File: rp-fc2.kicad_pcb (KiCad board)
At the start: 4 copper layers, 45 x 75 mm, 32 parts, among them CN1 20021521-00010T1LF, SW1 SW_Push, U1 RP2350A-QFN60, U2 W25Q128JVS, Y1 Crystal_GND24

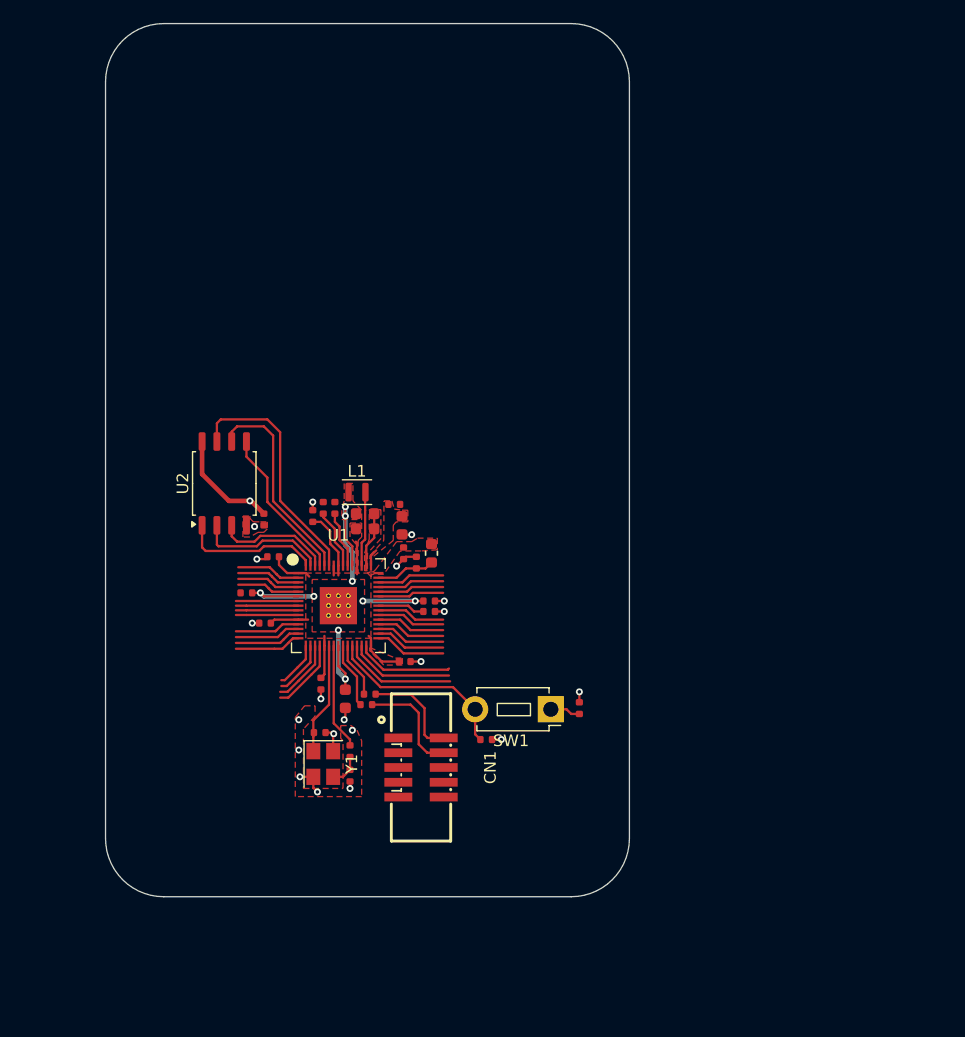
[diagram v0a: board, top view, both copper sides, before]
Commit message: rp2350 power + servo rails
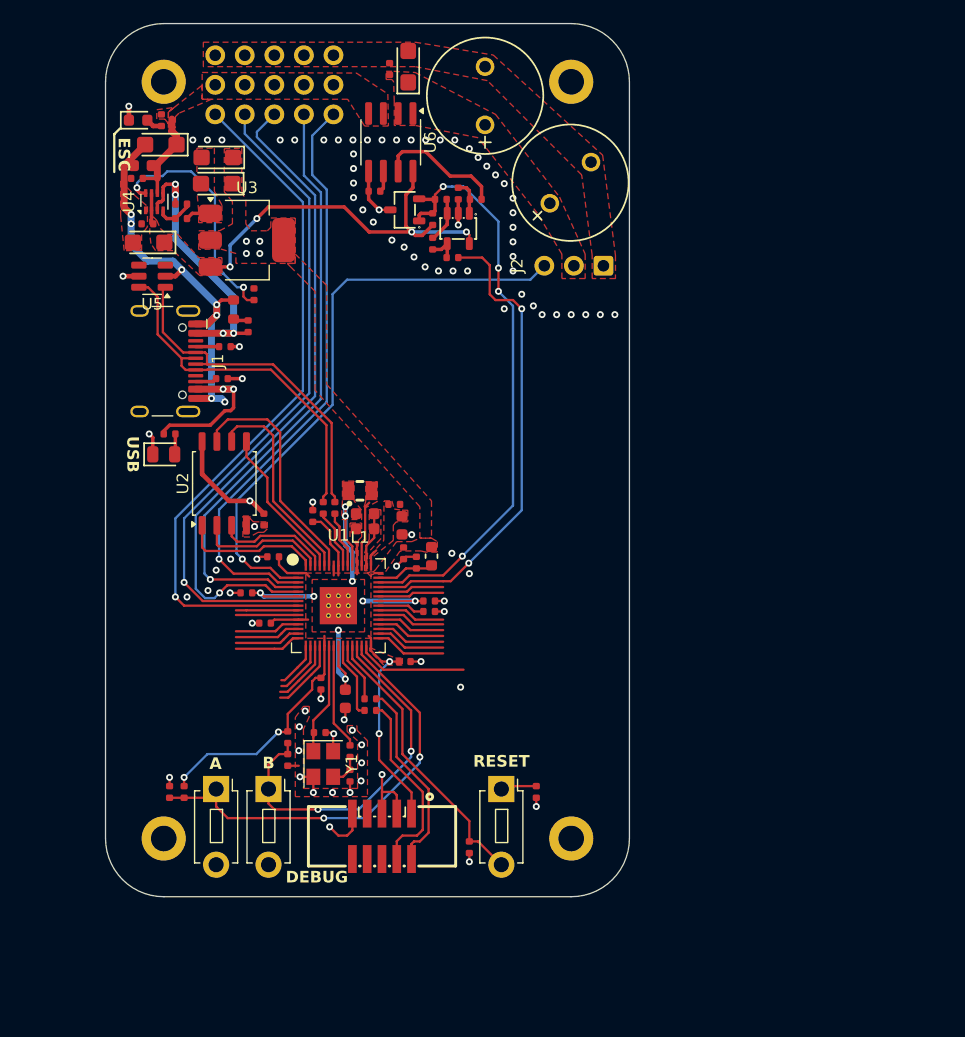
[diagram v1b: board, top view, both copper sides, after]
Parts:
- added C19: 100nF, PCM_JLCPCB:C_0402, F.Cu at (103.6, 92.2)
- added C20: 10uF, PCM_JLCPCB:C_CASE-A-3216-18(mm), F.Cu at (103.7, 93.8)
- added C21: 10uF, PCM_JLCPCB:C_CASE-A-3216-18(mm), F.Cu at (109.6, 86.5)
- added C22: 10uF, PCM_JLCPCB:C_CASE-A-3216-18(mm), F.Cu at (109.5, 88.8)
- added C23: 10uF, PCM_JLCPCB:C_CASE-A-3216-18(mm), F.Cu at (126.0, 78.7)
- added C24: 470uF, PCM_JLCPCB:C_Plugin,D10xL16mm, F.Cu at (132.6, 81.2)
- added C25: 470uF, PCM_JLCPCB:C_Plugin,D10xL16mm, F.Cu at (139.9, 88.7)
- added C26: 100nF, PCM_JLCPCB:C_0402, F.Cu at (124.4, 78.9)
- added C27: 100nF, PCM_JLCPCB:C_0402, F.Cu at (123.1, 89.4)
- added C28: 100nF, PCM_JLCPCB:C_0402, F.Cu at (102.7, 88.3)
- added C29: 2.2uF, PCM_JLCPCB:C_0603, F.Cu at (103.2, 87.2)
- added C30: 10uF, PCM_JLCPCB:C_CASE-A-3216-18(mm), F.Cu at (104.8, 85.4)
- added C31: 100nF, PCM_JLCPCB:C_0402, F.Cu at (105.5, 141.0)
- added C32: 100nF, PCM_JLCPCB:C_0402, F.Cu at (115.7, 138.2)
- added D1: Red, PCM_JLCPCB:D_0805, F.Cu at (105.0, 112.0)
- added D2: Red, PCM_JLCPCB:D_0603, F.Cu at (102.8, 83.3)
- added H1: MountingHole_Pad, MountingHole:MountingHole_2.2mm_M2_DIN965_Pad, F.Cu at (105.0, 80.0)
- added H2: MountingHole_Pad, MountingHole:MountingHole_2.2mm_M2_DIN965_Pad, F.Cu at (140.0, 80.0)
- added H3: MountingHole_Pad, MountingHole:MountingHole_2.2mm_M2_DIN965_Pad, F.Cu at (105.0, 145.0)
- added H4: MountingHole_Pad, MountingHole:MountingHole_2.2mm_M2_DIN965_Pad, F.Cu at (140.0, 145.0)
- added J1: USB_C_Receptacle_USB2.0_16P, Connector_USB:USB_C_Receptacle_HCTL_HC-TYPE-C-16P-01A, F.Cu at (104.0, 104.0)
- added J2: Conn_01x03, Connector_PinHeader_2.54mm:PinHeader_1x03_P2.54mm_Vertical, F.Cu at (137.7, 95.8)
- added J3: Conn_01x05, Connector_PinHeader_2.54mm:PinHeader_1x05_P2.54mm_Vertical, F.Cu at (109.4, 82.8)
- added J4: Conn_01x05, Connector_PinHeader_2.54mm:PinHeader_1x05_P2.54mm_Vertical, F.Cu at (109.4, 80.3)
- added J5: Conn_01x05, Connector_PinHeader_2.54mm:PinHeader_1x05_P2.54mm_Vertical, F.Cu at (109.4, 77.7)
- added R10: 220Ω, PCM_JLCPCB:R_0402, F.Cu at (105.5, 110.2)
- added R11: 5.1kΩ, PCM_JLCPCB:R_0402, F.Cu at (110.0, 105.5)
- added R12: 10kΩ, PCM_JLCPCB:R_0402, F.Cu at (106.5, 91.8)
- added R13: 10kΩ, PCM_JLCPCB:R_0402, F.Cu at (112.8, 98.2)
- added R14: 33kΩ, PCM_JLCPCB:R_0402, F.Cu at (112.2, 101.0)
- added R15: 82kΩ, PCM_JLCPCB:R_0603, F.Cu at (111.0, 99.6)
- added R16: 10kΩ, PCM_JLCPCB:R_0402, F.Cu at (131.8, 90.1)
- added R17: 27kΩ, PCM_JLCPCB:R_0402, F.Cu at (130.3, 89.6)
- added R18: 680Ω, PCM_JLCPCB:R_0402, F.Cu at (128.1, 91.8)
- added R19: 220Ω, PCM_JLCPCB:R_0402, F.Cu at (129.8, 95.1)
- added R20: 10kΩ, PCM_JLCPCB:R_0402, F.Cu at (128.8, 90.1)
- added R21: 27kΩ, PCM_JLCPCB:R_0402, F.Cu at (128.1, 93.9)
- added R22: 220Ω, PCM_JLCPCB:R_0402, F.Cu at (104.8, 83.3)
- added R23: 10kΩ, PCM_JLCPCB:R_0402, F.Cu at (106.8, 141.0)
- added R24: 10kΩ, PCM_JLCPCB:R_0402, F.Cu at (115.7, 136.3)
- added R8: 5.1kΩ, PCM_JLCPCB:R_0402, F.Cu at (110.2, 102.8)
- added R9: 10kΩ, PCM_JLCPCB:R_0402, F.Cu at (106.5, 90.5)
- added SW2: SW_Push, Button_Switch_THT:SW_PUSH_1P1T_6x3.5mm_H4.3_APEM_MJTP1243, F.Cu at (109.5, 140.8)
- added SW3: SW_Push, Button_Switch_THT:SW_PUSH_1P1T_6x3.5mm_H4.3_APEM_MJTP1243, F.Cu at (114.0, 140.8)
- added U3: AMS1117-3.3, Package_TO_SOT_SMD:SOT-223-3_TabPin2, F.Cu at (112.2, 93.6)
- added U4: TPS2116DRL, Package_TO_SOT_SMD:SOT-583-8, F.Cu at (104.2, 90.3)
- added U5: SRV05-4, Package_TO_SOT_SMD:SOT-23-6, F.Cu at (104.0, 96.7)
- added U6: ACS712xLCTR-05B, Package_SO:SOIC-8_3.9x4.9mm_P1.27mm, F.Cu at (124.5, 85.2)
- added U7: LMV321IDBVR, PCM_JLCPCB:SOT-23-5_L3.0-W1.7-P0.95-LS2.8-BR, F.Cu at (130.3, 92.6)
- added U8: CJ431, PCM_JLCPCB:SOT-23-3_L2.9-W1.6-P1.90-LS2.8-BR, F.Cu at (125.7, 91.0)
- L1: value 3.3u -> AOTA-B201610S3R3-101-T; footprint Inductor_SMD:L_Murata_DFE201610P -> easyeda2kicad:IND-SMD_L2.0-W1.6_AOTA-B201610S3R3-101-T
- moved C18 9.36 mm to (131.2, 145.8), turned to -90 degrees
- moved R4 8.10 mm to (137.0, 141.0), turned to 90 degrees
- moved SW1 8.06 mm to (134.0, 140.8), turned to -90 degrees
- moved CN1 6.80 mm to (123.7, 144.8), turned to 180 degrees
- moved R6 0.61 mm to (122.8, 134.0)
- moved R7 0.40 mm to (122.8, 133.0)
- moved L1 0.28 mm to (121.8, 115.1), turned to 180 degrees
- moved FB1 0.25 mm to (128.0, 120.8)
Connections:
- CN1 pad 7: GND -> unconnected-(CN1-Pad7)
- L1 pad 1: +1V1 -> Net-(U1-VREG_LX)
- L1 pad 2: Net-(U1-VREG_LX) -> +1V1
- U1 pad 2: unconnected-(U1-GPIO0-Pad2) -> CH1
- U1 pad 27: unconnected-(U1-GPIO16-Pad27) -> USR_SW1
- U1 pad 28: unconnected-(U1-GPIO17-Pad28) -> USR_SW2
- U1 pad 3: unconnected-(U1-GPIO1-Pad3) -> CH6
- U1 pad 4: unconnected-(U1-GPIO2-Pad4) -> CH5
- U1 pad 42: unconnected-(U1-GPIO28_ADC2-Pad42) -> I_COND
- U1 pad 43: unconnected-(U1-GPIO29_ADC3-Pad43) -> I_COND_2_5
- U1 pad 5: unconnected-(U1-GPIO3-Pad5) -> CH4
- U1 pad 7: unconnected-(U1-GPIO4-Pad7) -> CH3
- U1 pad 8: unconnected-(U1-GPIO5-Pad8) -> CH2
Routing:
- net GND: track 21.4 -> 84.6 mm, vias 20 -> 97
- net CH2: track 0.00 -> 60.0 mm, vias 0 -> 1
- net CH4: track 0.00 -> 57.5 mm, vias 0 -> 1
- net CH3: track 0.00 -> 57.4 mm, vias 0 -> 1
- net CH5: track 0.00 -> 52.7 mm, vias 0 -> 1
- net CH1: track 0.00 -> 51.1 mm, vias 0 -> 1
- net I_COND_2_5: track 0.00 -> 51.0 mm, vias 0 -> 4
- net CH6: track 0.00 -> 50.9 mm, vias 0 -> 1
- net I_COND: track 0.00 -> 41.1 mm, vias 0 -> 2
- net /Power/USB_VBUS: track 0.00 -> 39.7 mm, vias 0 -> 7
- net +5V: track 0.00 -> 37.9 mm, vias 0 -> 4
- net USR_SW2: track 0.00 -> 37.8 mm, vias 0 -> 2
- net USR_SW1: track 0.00 -> 32.1 mm, vias 0 -> 2
- net +3V3: track 38.1 -> 70.0 mm, vias 1 -> 9
- net USB_D+: track 0.00 -> 31.2 mm
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- added copper zone on F.Cu, net +5V
- added copper zone on F.Cu, net /Power/VBUCK_IN
- added copper zone on F.Cu, net Net-(U1-VREG_LX)
- added copper zone on F.Cu, net VBUCK
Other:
- board text added: "A"
- board text added: "B"
- board text added: "DEBUG"
- board text added: "ESC"
- board text added: "RESET"
- board text added: "USB"

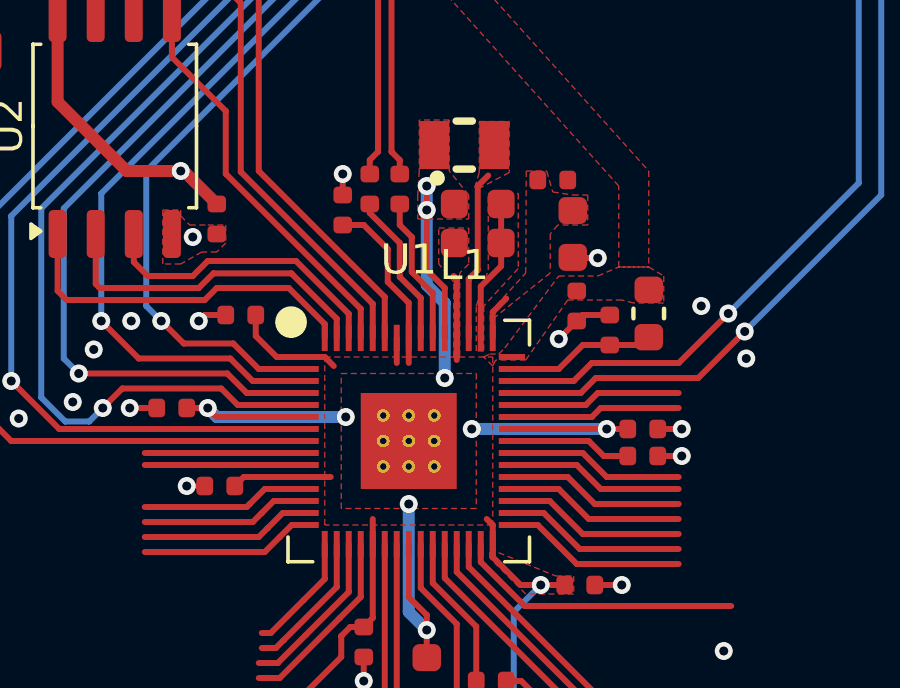
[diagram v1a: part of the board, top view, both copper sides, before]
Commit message: 3v3 rail thicker
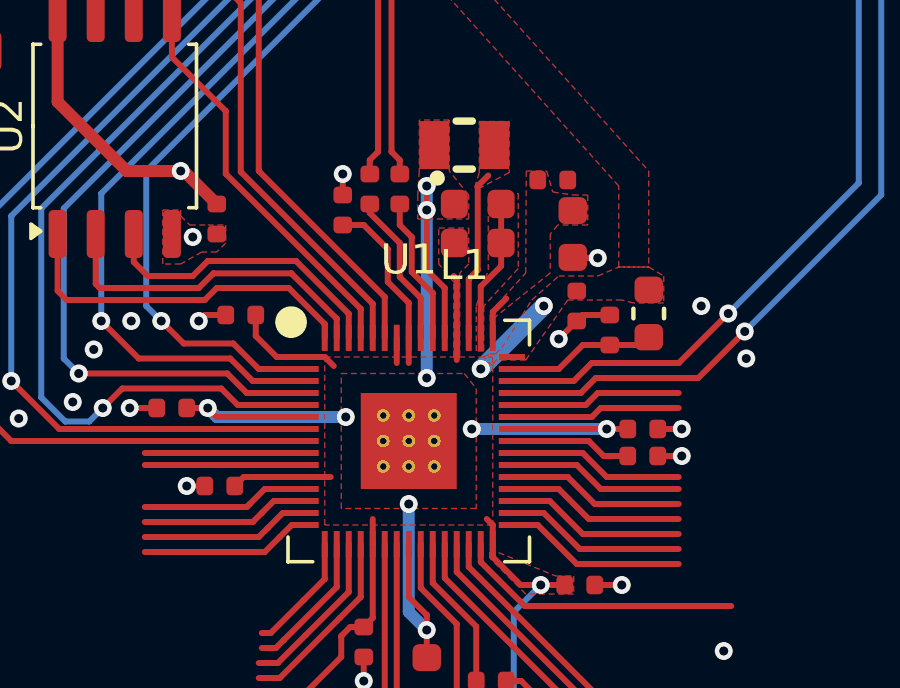
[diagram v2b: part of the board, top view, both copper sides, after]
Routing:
- net +3V3: track 70.0 -> 73.0 mm, vias 9 -> 11
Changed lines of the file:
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@@
 			(dashed_line_gap_ratio 3.000000)
 			(svgprecision 4)
-			(plotframeref no)
+			(plotframeref yes)
 			(viasonmask no)
 			(mode 1)
@@
 	)
 	(via
+		(at 122.4 122.6)
+		(size 0.6)
+		(drill 0.3)
+		(layers "F.Cu" "B.Cu")
+		(free yes)
+		(net 3)
+	)
+	(via
+		(at 124.5 120.5)
+		(size 0.6)
+		(drill 0.3)
+		(layers "F.Cu" "B.Cu")
+		(free yes)
+		(net 3)
+	)
+	(via
 		(at 113.25 93.7)
 		(size 0.6)
@@
 	)
 	(segment
+		(start 124.5 120.5)
+		(end 122.4 122.6)
+		(width 0.6)
+		(layer "B.Cu")
+		(net 3)
+	)
+	(segment
 		(start 114.85 135.85)
 		(end 112.95 137.75)
@@
 	)
 	(via
-		(at 121.2 122.9)
+		(at 120.6 122.899998)
 		(size 0.6)
 		(drill 0.3)
@@
 	)
 	(segment
-		(start 120.6 119.8)
-		(end 121.2 120.4)
-		(width 0.4)
-		(layer "B.Cu")
-		(net 4)
-	)
-	(segment
-		(start 121.2 120.4)
-		(end 121.2 122.9)
-		(width 0.4)
-		(layer "B.Cu")
-		(net 4)
-	)
-	(segment
 		(start 122.1 124.6)
 		(end 126.6 124.6)
@@
 	)
 	(segment
-		(start 113.3 123.9)
-		(end 113.6 124.2)
+		(start 120.6 122.899998)
+		(end 120.6 116.5)
 		(width 0.4)
 		(layer "B.Cu")
@@
 	)
 	(segment
-		(start 120.6 116.5)
-		(end 120.6 119.8)
+		(start 113.3 123.9)
+		(end 113.6 124.2)
 		(width 0.4)
 		(layer "B.Cu")
@@
 		(polygon
 			(pts
-				(xy 117.75 122.75) (xy 122.25 122.75) (xy 122.25 127.25) (xy 117.75 127.25)
+				(xy 117.75 122.75) (xy 121.85 122.75) (xy 122.25 123.25) (xy 122.25 127.25) (xy 117.75 127.25)
 			)
 		)
@@
 		(polygon
 			(pts
-				(xy 122.5 122.2) (xy 122.7 122.1) (xy 123 122.1) (xy 123.2 121.9) (xy 125 119.5) (xy 126.3 119.5)
-				(xy 127 119.2) (xy 128 119.2) (xy 128.5 119.5) (xy 128.5 120.4) (xy 127.5 120.4) (xy 127.1 120.3)
-				(xy 125.3 120.3) (xy 123.9 122.3) (xy 122.9 122.3) (xy 122.8 122.5)
+				(xy 122.5 122.2) (xy 122.7 122.1) (xy 122.9 122.1) (xy 123.1 121.9) (xy 124.1 120.3) (xy 125 119.5)
+				(xy 126.3 119.5) (xy 127 119.2) (xy 128 119.2) (xy 128.5 119.5) (xy 128.5 120.4) (xy 127.5 120.4)
+				(xy 127.1 120.3) (xy 125.3 120.3) (xy 123.9 122.3) (xy 122.9 122.3) (xy 122.8 122.5)
 			)
 		)

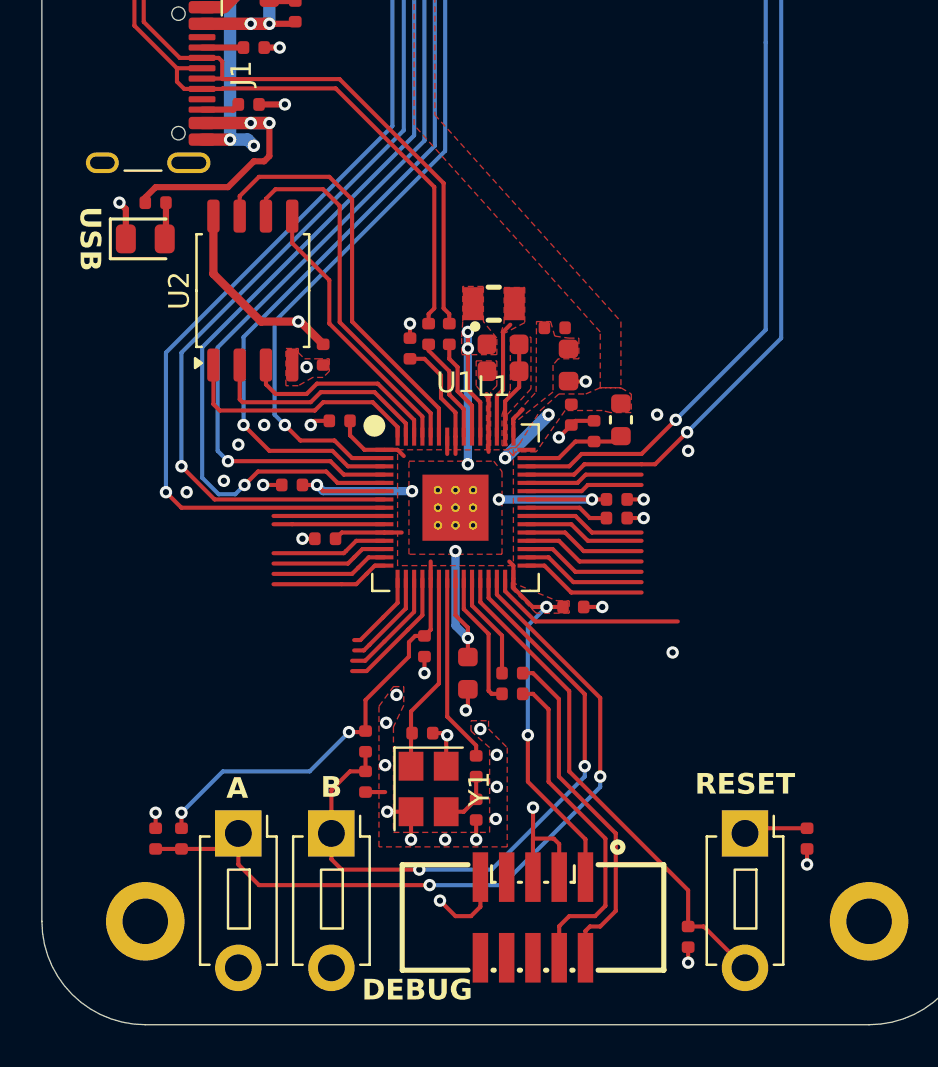
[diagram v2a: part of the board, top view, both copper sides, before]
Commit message: add camera breakout
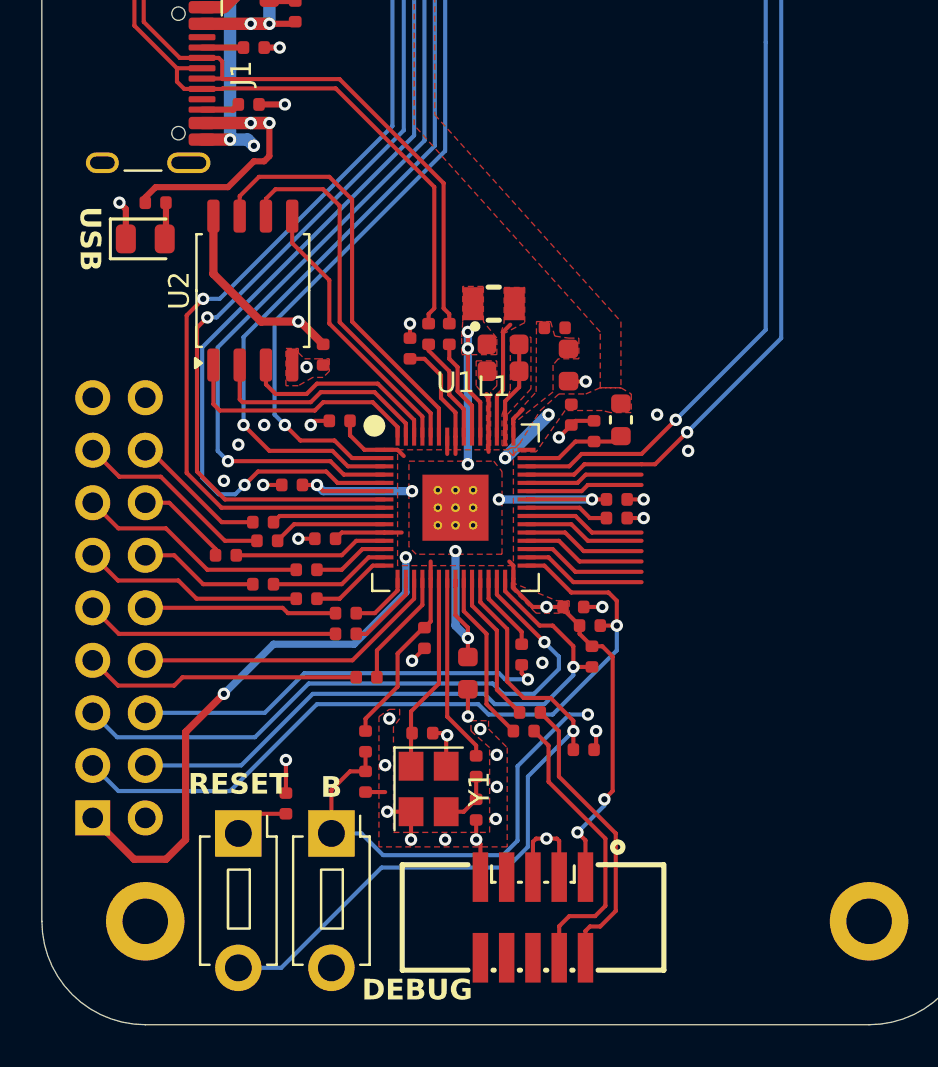
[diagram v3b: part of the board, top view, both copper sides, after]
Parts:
- removed C31: 100nF, PCM_JLCPCB:C_0402
- removed SW2: SW_Push, Button_Switch_THT:SW_PUSH_1P1T_6x3.5mm_H4.3_APEM_MJTP1243
- added J6: OV7670 Breakout, Connector_PinHeader_2.54mm:PinHeader_2x09_P2.54mm_Vertical, B.Cu at (102.5, 140.0)
- added R25: 22Ω, PCM_JLCPCB:R_0402, F.Cu at (110.9, 126.6)
- added R26: 22Ω, PCM_JLCPCB:R_0402, F.Cu at (108.9, 127.3)
- added R27: 22Ω, PCM_JLCPCB:R_0402, F.Cu at (112.8, 128.0)
- added R28: 22Ω, PCM_JLCPCB:R_0402, F.Cu at (110.7, 128.7)
- added R29: 22Ω, PCM_JLCPCB:R_0402, F.Cu at (112.8, 129.4)
- added R30: 22Ω, PCM_JLCPCB:R_0402, F.Cu at (114.7, 130.1)
- added R31: 22Ω, PCM_JLCPCB:R_0402, F.Cu at (114.7, 131.1)
- added R32: 22Ω, PCM_JLCPCB:R_0402, F.Cu at (115.7, 133.2)
- added R33: 22Ω, PCM_JLCPCB:R_0402, F.Cu at (123.2, 132.1)
- added R34: 4.7kΩ, PCM_JLCPCB:R_0402, F.Cu at (126.6, 132.2)
- added R35: 4.7kΩ, PCM_JLCPCB:R_0402, F.Cu at (126.5, 130.7)
- R23: value 10kΩ -> 22Ω
- moved R4 25.3 mm to (111.8, 139.3), turned to -90 degrees
- moved SW1 24.5 mm to (109.5, 140.8)
- moved R23 15.8 mm to (110.7, 125.7), turned to 180 degrees
- moved C18 10.4 mm to (126.2, 136.7), turned to 0 degrees
- moved R7 2.08 mm to (123.6, 134.9)
- moved R6 1.88 mm to (123.3, 135.8)
- moved C13 0.40 mm to (118.5, 131.3)
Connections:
- R23 pad 1: USR_SW2 -> Net-(U1-GPIO6)
- R23 pad 2: +3V3 -> D0
- U1 pad 10: unconnected-(U1-GPIO7-Pad10) -> Net-(U1-GPIO7)
- U1 pad 12: unconnected-(U1-GPIO8-Pad12) -> Net-(U1-GPIO8)
- U1 pad 13: unconnected-(U1-GPIO9-Pad13) -> Net-(U1-GPIO9)
- U1 pad 14: unconnected-(U1-GPIO10-Pad14) -> Net-(U1-GPIO10)
- U1 pad 15: unconnected-(U1-GPIO11-Pad15) -> Net-(U1-GPIO11)
- U1 pad 16: unconnected-(U1-GPIO12-Pad16) -> Net-(U1-GPIO12)
- U1 pad 17: unconnected-(U1-GPIO13-Pad17) -> Net-(U1-GPIO13)
- U1 pad 18: unconnected-(U1-GPIO14-Pad18) -> XCLK
- U1 pad 19: unconnected-(U1-GPIO15-Pad19) -> Net-(U1-GPIO15)
- U1 pad 27: USR_SW1 -> Net-(U1-GPIO16)
- U1 pad 28: USR_SW2 -> VSYNC
- U1 pad 29: unconnected-(U1-GPIO18-Pad29) -> SIO_D
- U1 pad 31: unconnected-(U1-GPIO19-Pad31) -> SIO_C
- U1 pad 32: unconnected-(U1-GPIO20-Pad32) -> USR_SW1
- U1 pad 9: unconnected-(U1-GPIO6-Pad9) -> Net-(U1-GPIO6)
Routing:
- net USR_SW2: track 37.8 -> 0.00 mm, vias 2 -> 0
- net SIO_C: track 0.00 -> 37.4 mm, vias 0 -> 1
- net VSYNC: track 0.00 -> 30.4 mm, vias 0 -> 1
- net SIO_D: track 0.00 -> 30.2 mm, vias 0 -> 1
- net HREF: track 0.00 -> 20.2 mm, vias 0 -> 1
- net XCLK: track 0.00 -> 15.2 mm
- net +3V3: track 73.0 -> 88.2 mm, vias 11 -> 12
- net PCLK: track 0.00 -> 13.4 mm
- net D7: track 0.00 -> 12.3 mm
- net D3: track 0.00 -> 11.2 mm
- net D5: track 0.00 -> 10.7 mm
- net D1: track 0.00 -> 9.75 mm
- net unconnected-(U1-GPIO18-Pad29): track 9.55 -> 0.00 mm
- net D6: track 0.00 -> 9.31 mm
- net Net-(U1-RUN): track 24.6 -> 33.8 mm, vias 0 -> 1
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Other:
- board text removed: "A"
